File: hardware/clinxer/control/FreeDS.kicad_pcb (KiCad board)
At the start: 2 copper layers, 61 x 93 mm, 27 parts, among them J1 Conn_01x04, J2 VENTILADOR, J3 SALIDAS AUXILIARES, J4 Conn_01x03_Male, J5 Conn_01x03_Male, J6 Conn_01x03_Male, J7 Conn_01x02_Pin, Q1 DS18B20, Q2 BC337, SW1 PRG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

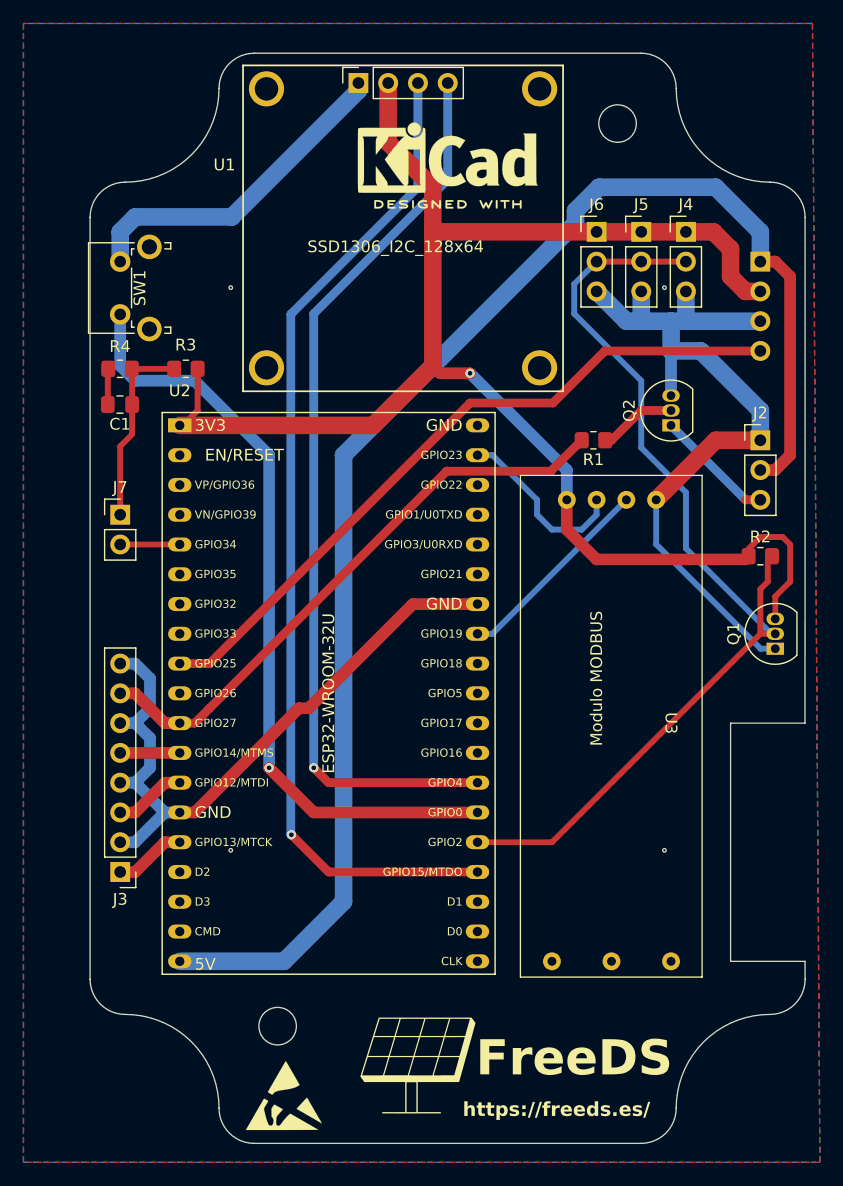
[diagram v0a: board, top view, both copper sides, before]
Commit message: Correcciones en arquitectura clinxer
Signed-off-by: Iván Sánchez Ortega <ivan@sanchezortega.es>
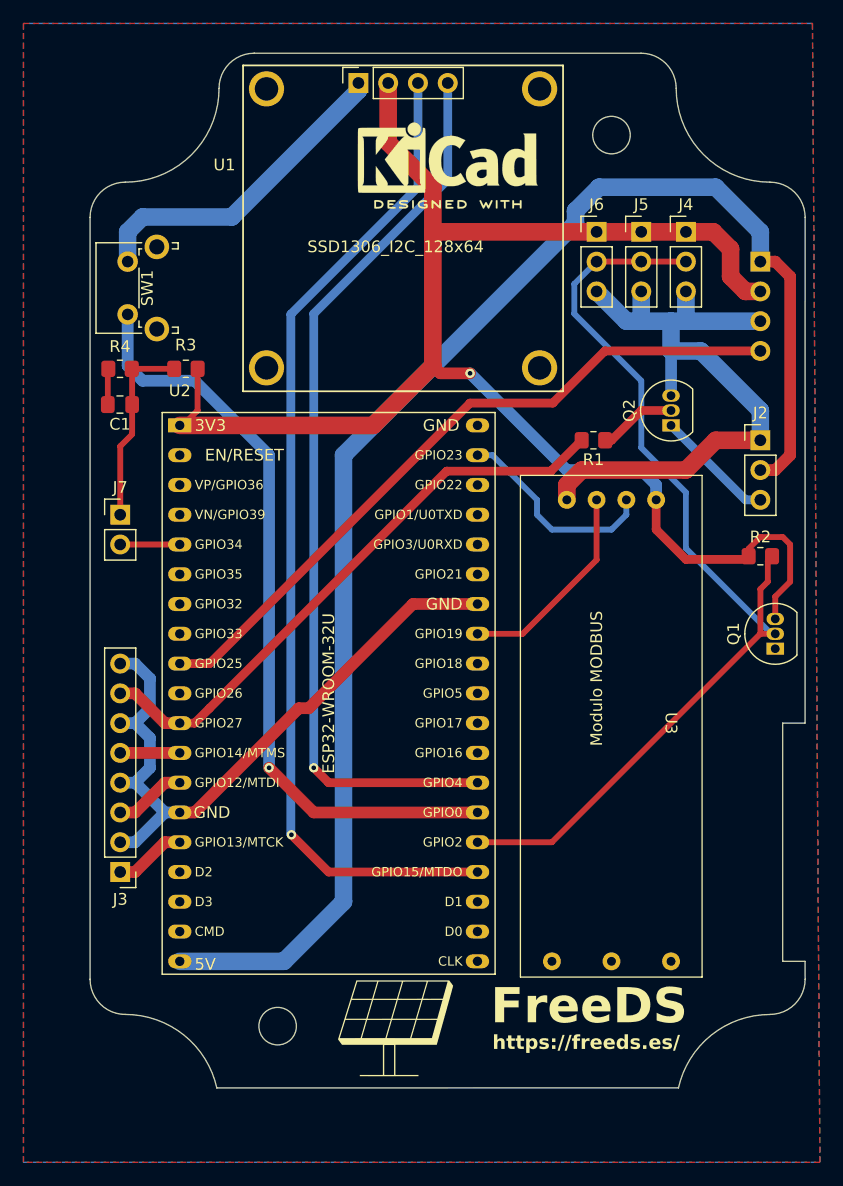
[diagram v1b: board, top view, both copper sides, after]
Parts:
- removed H2, H3, H4, H5: MountingHole, MountingHole:MountingHole_3.2mm_M3
- removed the REF** at (92.7, 139.7)
- moved FreeDS 3.70 mm to (102.2, 134.0)
- moved H1 1.11 mm to (120.7, 57.8)
- moved SW1 0.64 mm to (79.4, 73.1)
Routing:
- net /GND: track 157.5 -> 147.6 mm
- net /TX: track 15.3 -> 17.9 mm
- net /3V3: track 135.0 -> 133.9 mm
- net /SW1: track 66.3 -> 65.6 mm
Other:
- board size 61 x 93 mm -> 61 x 88.3 mm
